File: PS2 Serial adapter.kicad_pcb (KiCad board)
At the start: 2 copper layers, 36.5 x 18 mm, 11 parts, among them J1 PS2, J2 PC, U1 MAX3323EEUE

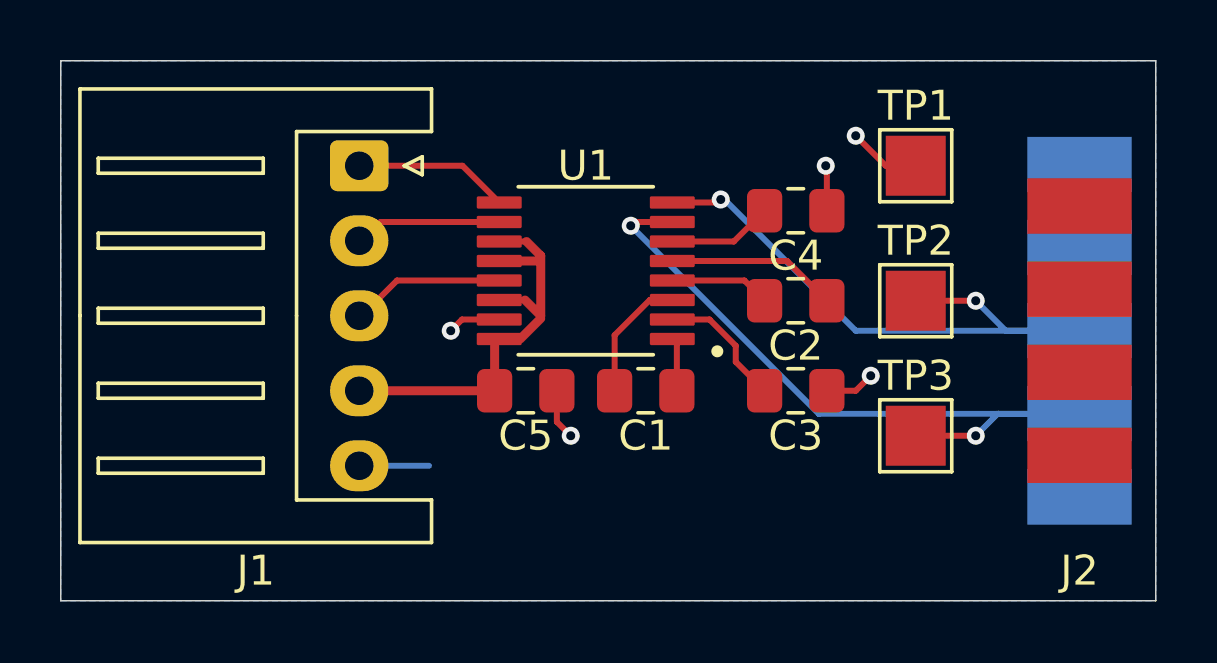
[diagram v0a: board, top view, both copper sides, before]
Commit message: Fillet corners, add missing labels, fix trace
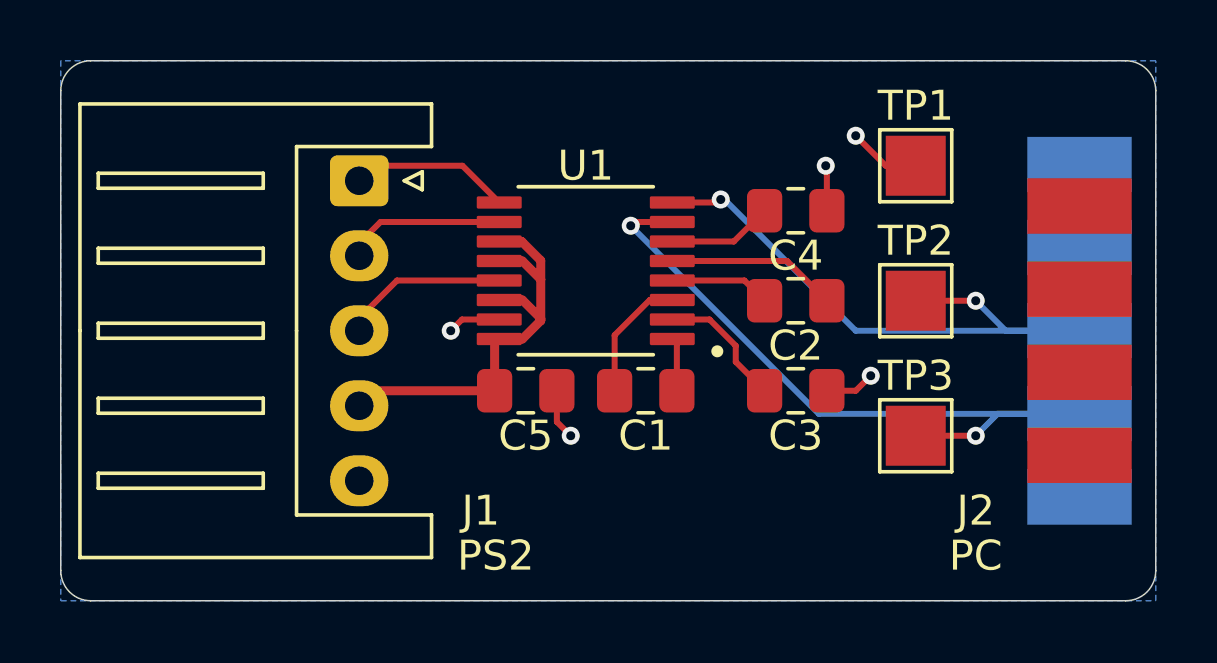
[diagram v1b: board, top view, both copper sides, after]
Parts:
- moved J1 0.50 mm to (127.5, 55.0)
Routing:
- net GND: track 11.3 -> 9.06 mm
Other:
- outline, holes or cut-outs redrawn
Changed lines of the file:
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@@
 	(footprint "Connector_JST:JST_XH_S5B-XH-A_1x05_P2.50mm_Horizontal"
 		(layer "F.Cu")
-		(at 127.45 54.5 -90)
+		(at 127.45 55 -90)
 		(descr "JST XH series connector, S5B-XH-A (http://www.jst-mfg.com/product/pdf/eng/eXH.pdf), generated with kicad-footprint-generator")
 		(tags "connector JST XH horizontal")
 		(property "Reference" "J1"
-			(at 13.5 3.45 0)
+			(at 11 -4.05 0)
 			(layer "F.SilkS")
 			(effects
@@
 		)
 		(property "Value" "PS2"
-			(at 13.5 -0.05 0)
-			(layer "F.Fab")
+			(at 12.5 -4.55 0)
+			(layer "F.SilkS")
 			(effects
 				(font
@@
 		)
 		(fp_text user "${REFERENCE}"
-			(at 13.5 3.45 0)
+			(at 11 -4.05 0)
 			(layer "F.Fab")
 			(effects
@@
 		(tags "9-pin D-Sub connector edge mount solder cup socket x-pin-pitch 2.77mm mounting holes distance 25mm")
 		(property "Reference" "J2"
-			(at 8 0 0)
+			(at 6 3.4575 0)
 			(layer "F.SilkS")
 			(effects
@@
 		)
 		(property "Value" "PC"
-			(at 8 2.9575 0)
-			(layer "F.Fab")
+			(at 7.5 3.4575 0)
+			(layer "F.SilkS")
 			(effects
 				(font
@@
 		)
 	)
-	(gr_rect
-		(start 117.5 51)
-		(end 154 69)
+	(gr_line
+		(start 154 52)
+		(end 154 68)
+		(stroke
+			(width 0.05)
+			(type default)
+		)
+		(layer "Edge.Cuts")
+	)
+	(gr_arc
+		(start 118.5 69)
+		(mid 117.792893 68.707107)
+		(end 117.5 68)
+		(stroke
+			(width 0.05)
+			(type default)
+		)
+		(layer "Edge.Cuts")
+	)
+	(gr_arc
+		(start 153 51)
+		(mid 153.707107 51.292893)
+		(end 154 52)
+		(stroke
+			(width 0.05)
+			(type default)
+		)
+		(layer "Edge.Cuts")
+	)
+	(gr_line
+		(start 118.5 51)
+		(end 153 51)
+		(stroke
+			(width 0.05)
+			(type default)
+		)
+		(layer "Edge.Cuts")
+	)
+	(gr_line
+		(start 153 69)
+		(end 118.5 69)
+		(stroke
+			(width 0.05)
+			(type default)
+		)
+		(layer "Edge.Cuts")
+	)
+	(gr_line
+		(start 117.5 68)
+		(end 117.5 52)
+		(stroke
+			(width 0.05)
+			(type default)
+		)
+		(layer "Edge.Cuts")
+	)
+	(gr_arc
+		(start 117.5 52)
+		(mid 117.792893 51.292893)
+		(end 118.5 51)
+		(stroke
+			(width 0.05)
+			(type default)
+		)
+		(layer "Edge.Cuts")
+	)
+	(gr_arc
+		(start 154 68)
+		(mid 153.707107 68.707107)
+		(end 153 69)
 		(stroke
 			(width 0.05)
 			(type default)
 		)
-		(fill no)
 		(layer "Edge.Cuts")
 	)
@@
 	)
 	(segment
-		(start 129.775054 64.5)
-		(end 127.5325 64.5)
-		(width 0.2)
-		(layer "B.Cu")
-		(net 6)
-	)
-	(segment
 		(start 139.9375 57.025)
 		(end 137.885 57.025)
@@
 	)
 	(segment
-		(start 133.325 57.675)
-		(end 133.5 57.5)
-		(width 0.2)
+		(start 132.887788 58.975)
+		(end 133.5 59.587212)
+		(width 0.3)
 		(layer "F.Cu")
 		(net 8)
 	)
 	(segment
-		(start 133.5 59.5)
-		(end 132.975 58.975)
+		(start 133.5 57.660001)
+		(end 133.5 58.287212)
 		(width 0.3)
 		(layer "F.Cu")
@@
 	)
 	(segment
-		(start 127.5325 62)
-		(end 131.9625 62)
+		(start 133.5 59.587212)
+		(end 133.5 59.662788)
 		(width 0.3)
 		(layer "F.Cu")
@@
 	)
 	(segment
-		(start 133.5 59.5)
-		(end 133.5 57.5)
+		(start 132.115 58.975)
+		(end 132.887788 58.975)
 		(width 0.3)
 		(layer "F.Cu")
@@
 	)
 	(segment
-		(start 132.817078 60.275)
-		(end 133.5 59.592078)
+		(start 132.864999 57.025)
+		(end 133.5 57.660001)
 		(width 0.3)
 		(layer "F.Cu")
@@
 	)
 	(segment
-		(start 131.9625 60.4275)
-		(end 132.115 60.275)
-		(width 0.2)
+		(start 127.5325 62)
+		(end 131.9625 62)
+		(width 0.3)
 		(layer "F.Cu")
 		(net 8)
@@
 	(segment
 		(start 132.115 57.675)
-		(end 133.325 57.675)
+		(end 132.887788 57.675)
+		(width 0.3)
+		(layer "F.Cu")
+		(net 8)
+	)
+	(segment
+		(start 133.5 59.662788)
+		(end 132.887788 60.275)
 		(width 0.3)
 		(layer "F.Cu")
@@
 	)
 	(segment
-		(start 132.115 60.275)
-		(end 132.817078 60.275)
+		(start 131.9625 60.4275)
+		(end 132.115 60.275)
 		(width 0.2)
 		(layer "F.Cu")
@@
 	)
 	(segment
-		(start 133.5 57.5)
-		(end 133.025 57.025)
+		(start 132.887788 60.275)
+		(end 132.115 60.275)
 		(width 0.3)
 		(layer "F.Cu")
@@
 	)
 	(segment
-		(start 133.025 57.025)
-		(end 132.115 57.025)
-		(width 0.2)
+		(start 133.5 58.287212)
+		(end 133.5 59.662788)
+		(width 0.3)
 		(layer "F.Cu")
 		(net 8)
 	)
 	(segment
-		(start 132.975 58.975)
-		(end 132.115 58.975)
-		(width 0.2)
+		(start 132.115 57.025)
+		(end 132.864999 57.025)
+		(width 0.3)
 		(layer "F.Cu")
 		(net 8)
 	)
 	(segment
-		(start 131.9625 62)
-		(end 131.9625 60.4275)
+		(start 132.887788 57.675)
+		(end 133.5 58.287212)
 		(width 0.3)
 		(layer "F.Cu")
@@
 	)
 	(segment
-		(start 133.5 59.592078)
-		(end 133.5 59.5)
-		(width 0.2)
+		(start 131.9625 62)
+		(end 131.9625 60.4275)
+		(width 0.3)
 		(layer "F.Cu")
 		(net 8)
